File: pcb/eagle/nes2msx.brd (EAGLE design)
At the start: 27.9 x 39.4 mm, 9 parts, among them J1 ICSP, U1 ATTINY44A-SSU

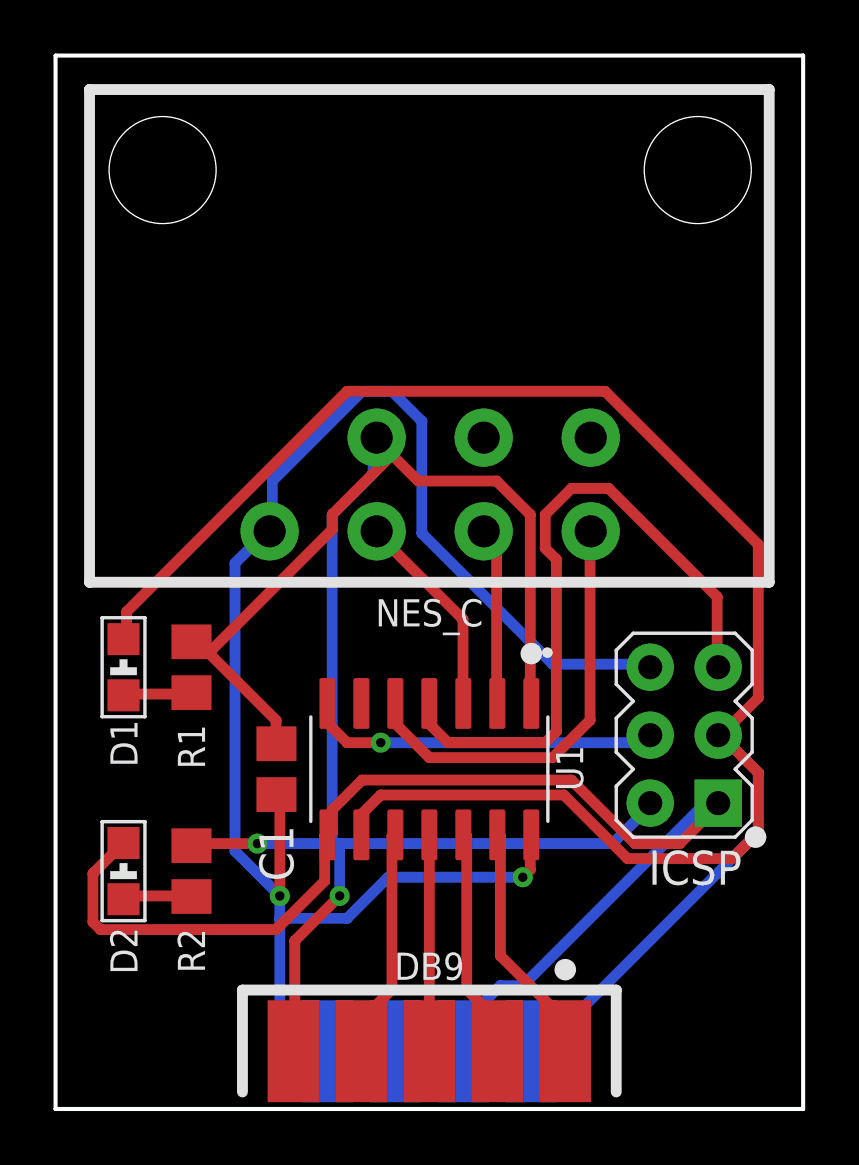
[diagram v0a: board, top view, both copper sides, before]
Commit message: Refactor Gerber files for nes2msx PCB design
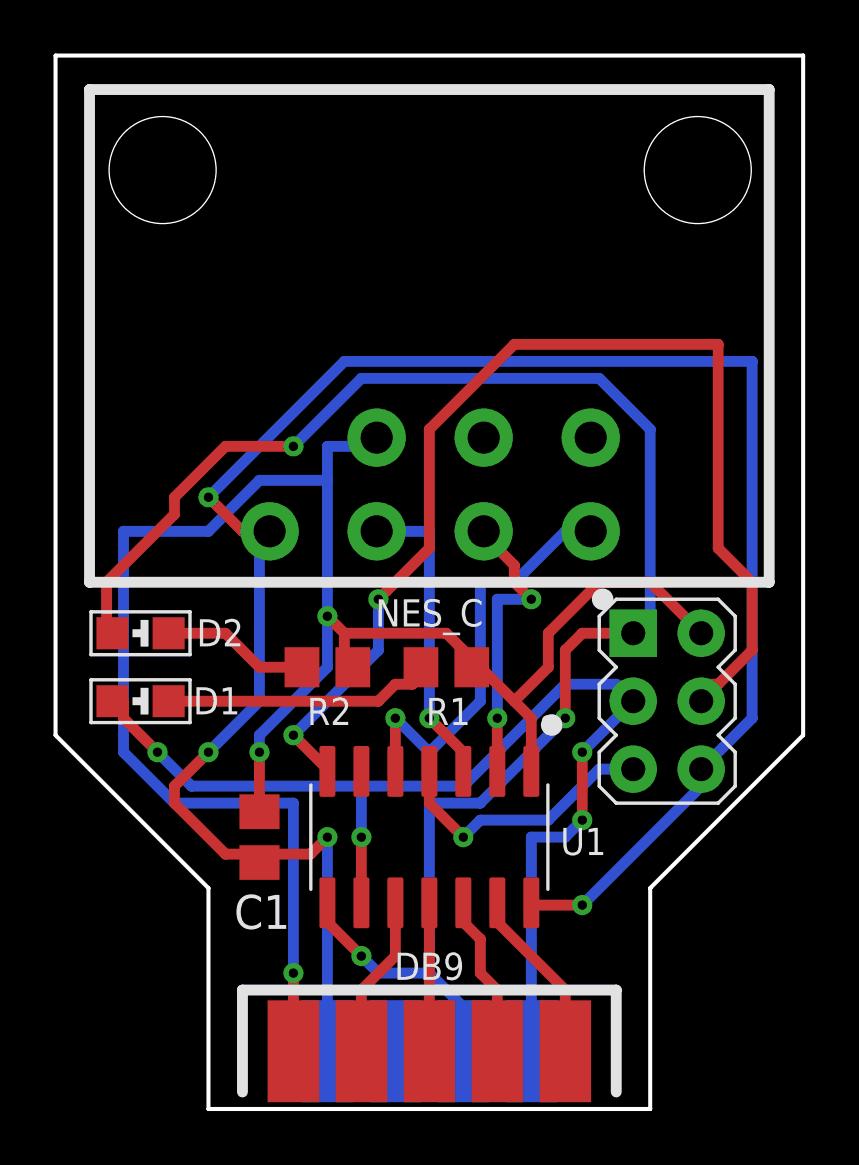
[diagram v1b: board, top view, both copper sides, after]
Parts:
- moved R1 9.53 mm to (14.6, 16.5), turned to 0 degrees
- moved R2 9.16 mm to (10.2, 16.5), turned to 0 degrees
- moved D2 8.91 mm to (3.17, 17.8), turned to 180 degrees
- moved C1 2.62 mm to (7.62, 10.2)
- moved U1 2.54 mm to (14.0, 10.2)
- moved D1 1.42 mm to (3.17, 15.2), turned to 180 degrees
- moved J1 1.42 mm to (22.9, 15.2), turned to 270 degrees
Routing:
- net SCK: track 76.1 -> 42.8 mm, vias 0 -> 4
- net MOSI: track 13.2 -> 42.5 mm, vias 1 -> 2
- net GND: track 61.0 -> 77.1 mm, vias 2 -> 4
- net MISO: track 46.4 -> 61.9 mm, vias 0 -> 3
- net RESET: track 25.4 -> 10.4 mm, vias 0 -> 1
- net N$9: track 2.57 -> 10.3 mm
- net N$6: track 6.64 -> 11.3 mm, vias 0 -> 2
- net N$5: track 7.77 -> 11.5 mm, vias 0 -> 1
- net N$10: track 2.60 -> 5.51 mm
- net N$4: track 8.64 -> 6.07 mm
- net N$2: track 8.64 -> 6.07 mm
- net N$1: track 9.16 -> 6.60 mm
- net N$3: track 8.09 -> 5.55 mm
- net VCC: track 72.4 -> 73.2 mm, vias 2 -> 3
- net N$7: track 16.2 -> 15.8 mm, vias 0 -> 1
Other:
- outline, holes or cut-outs redrawn
- board text removed: "ICSP"
